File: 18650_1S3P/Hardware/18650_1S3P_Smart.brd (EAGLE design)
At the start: 109.2 x 68.2 mm, 73 parts, among them J1 CONN_3MICROFIT_RT, J2 GEMS_POWER_PLUGOUTPUT, Q1 MOSFET-NCH-AON7522E, Q2 MOSFET-NCH-AON7522E, Q3 MOSFET-NCH-AON7522E, Q4 MOSFET-NCH-AON7522E, Q5 MOSFET-NCH-AON7522E, Q6 MOSFET-NCH-AON7522E, Q7 MOSFET_PCH-DMP2008, Q8 MOSFET_PCH-DMP2008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

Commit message: Continued layout of 1S3P Smart
Continued layout, connections made, labeling and cleanup required. Made fix to `ALERT` pin connection (had connected to `GND` erroneously vs `PACK-`)
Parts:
- moved C6 184.1 mm to (88.8, 42.5)
- moved C7 183.4 mm to (91.9, 42.5), turned to 180 degrees
- moved R27 179.5 mm to (88.8, 40.4), turned to 180 degrees
- moved D1 179.5 mm to (48.6, 16.4)
- moved R29 178.5 mm to (94.9, 38.5), turned to 270 degrees
- moved R28 176.4 mm to (88.8, 38.2)
- moved R30 174.1 mm to (94.9, 41.5), turned to 270 degrees
- moved C1 166.7 mm to (45.7, 12.6), turned to 90 degrees
- moved D2 161.0 mm to (48.6, 38.0)
- moved C2 155.5 mm to (45.7, 34.0), turned to 90 degrees
- moved U1 149.8 mm to (43.2, 12.7)
- moved R1 142.5 mm to (40.1, 9.65)
- moved R2 140.3 mm to (40.1, 7.62), turned to 180 degrees
- moved U2 137.6 mm to (43.2, 34.3)
- moved R3 134.9 mm to (40.1, 11.7)
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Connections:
- removed net GND: U4.12
- net PACK-: now also U4.12
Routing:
- net PACK-: track 2.35 -> 239.8 mm, vias 0 -> 4
- net PACK+: track 2.94 -> 192.0 mm, vias 2 -> 8
- net JUMP: track 0.00 -> 132.4 mm
- net SHDN: track 1.03 -> 104.8 mm, vias 1 -> 4
- net LED1: track 0.00 -> 80.5 mm, vias 0 -> 5
- net LED2: track 0.00 -> 53.6 mm, vias 0 -> 2
- net N$6: track 0.00 -> 45.2 mm, vias 0 -> 2
- net N$15: track 0.00 -> 45.2 mm, vias 0 -> 2
- net N$9: track 0.00 -> 44.5 mm, vias 0 -> 1
- net N$18: track 0.00 -> 44.5 mm, vias 0 -> 1
- net V_COM: track 0.00 -> 42.5 mm
- net SYS+: track 0.00 -> 36.7 mm, vias 0 -> 1
- net LED4: track 0.00 -> 36.0 mm, vias 0 -> 2
- net LED3: track 0.00 -> 31.9 mm, vias 0 -> 2
- net SYS-: track 0.00 -> 31.3 mm
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- added copper zone on layer 16, net N$15
- added copper zone on layer 16, net N$6

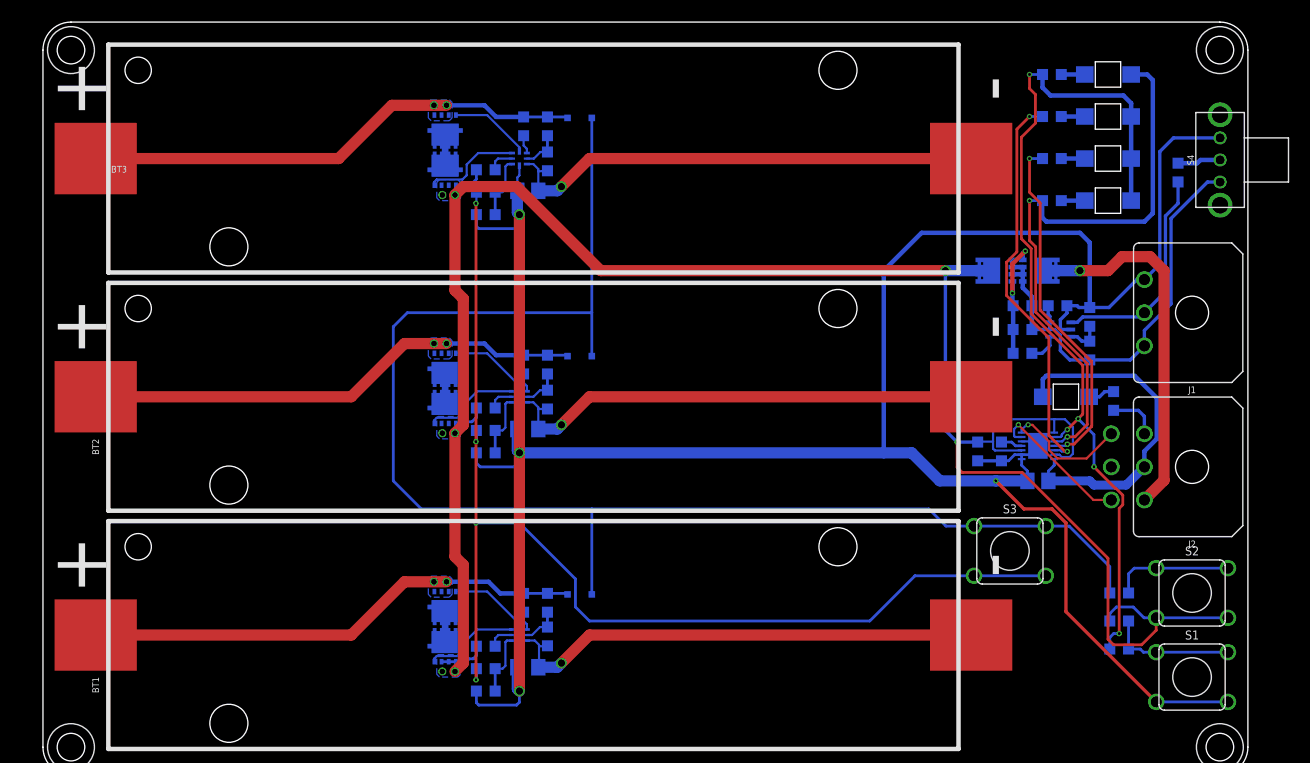
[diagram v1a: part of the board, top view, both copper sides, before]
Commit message: Layout and ref designator cleanup, ready for final verification
Continued layout cleanup, layout should be final barring final verification
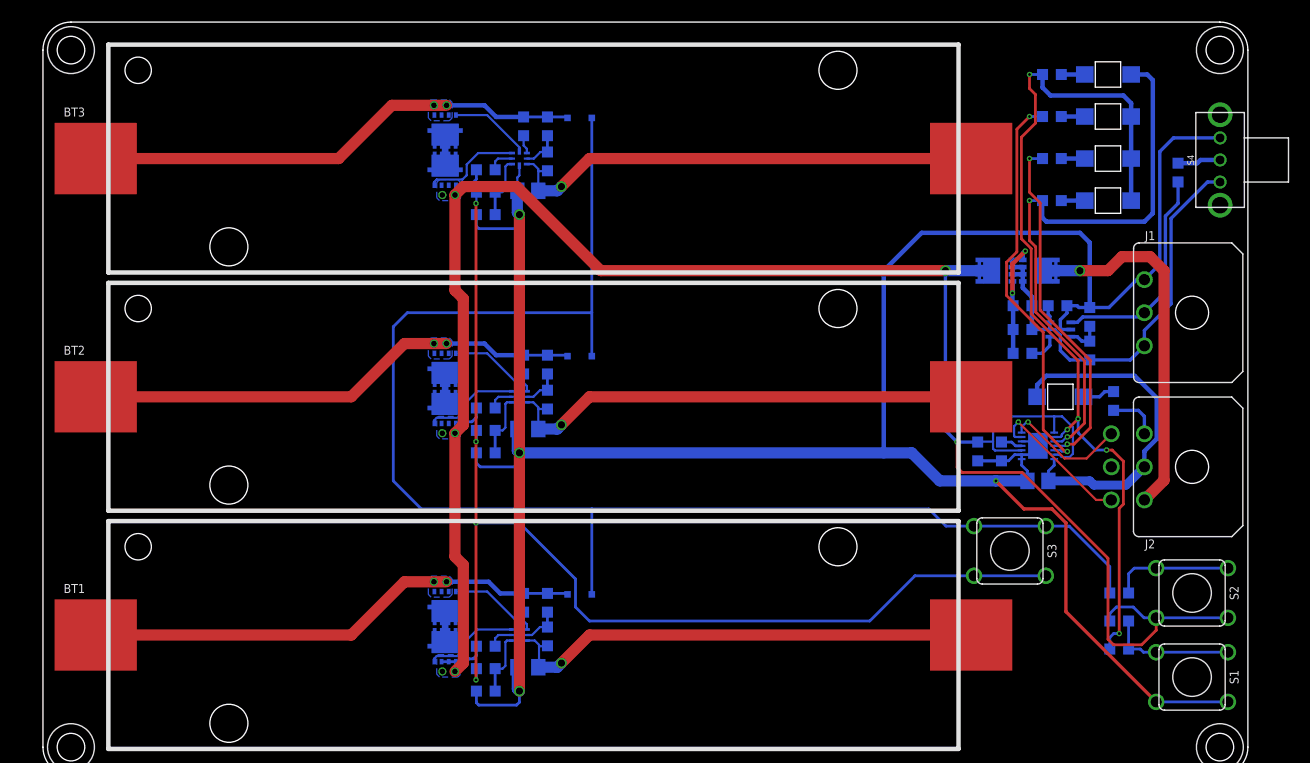
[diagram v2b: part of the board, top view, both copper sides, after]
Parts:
- BT1, BT2, BT3: value 186501042P -> 186501042P_NOSILK; device bschulz:BATT_1042P -> bschulz:BATT_1042P_NOSILK
- moved D8 0.51 mm to (92.2, 34.3)
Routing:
- net LED1: track 80.5 -> 81.1 mm
- net N$42: track 2.41 -> 2.92 mm
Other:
- board text added: "+"
- board text added: "-"
- board text added: "1S3P - Smart - 18650 Project Gonk Bobby Schulz v0.0"
- board text added: "CHARGE STAT"
- board text added: "INFO - Press to display battery charge state via CHARGE STAT LEDs JUMP - Press to "jump start" system on first insertion of batteries. System will start automatically if charger is applied SLEEP - Press and hold for > 6s in order to place the device in shutdown for shipping or storage. Must press JUMP or connect charger to start again"
